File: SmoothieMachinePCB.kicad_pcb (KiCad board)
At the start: 2 copper layers, 50 parts, among them J1 Up Button, J10 Vin, J11 LCD I2C Adapter, J2 Down Button, J3 Next Ingredient Button, J4 Next Recipe Button, J5 Solenoid Valve, J6 Stepper Motor 2, J8 Stepper Motor 1, J9 LoadCell, U1 ESP32-S3-WROOM-2, U2 FSA2567MPX, U3 DRV8825PWP, U4 VN10KN3-G, U6 NAU7802SGI, U7 XL1509-3.3

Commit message: Second round pcb files
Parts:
- moved H3 109.1 mm to (88.6, 144.1)
- moved C2 84.3 mm to (94.5, 56.5), turned to -90 degrees
- moved H1 83.6 mm to (88.6, 51.1)
- moved J6 79.4 mm to (125.0, 116.6), turned to 90 degrees
- moved R12 79.0 mm to (110.0, 138.5), turned to -90 degrees
- moved C11 78.6 mm to (93.5, 131.5), turned to -90 degrees
- moved J10 73.0 mm to (88.2, 74.0)
- moved R3 73.0 mm to (105.0, 108.6)
- moved C10 72.6 mm to (99.5, 127.5), turned to -90 degrees
- moved R8 71.5 mm to (108.0, 128.0), turned to -90 degrees
- moved C12 70.4 mm to (102.5, 135.5), turned to -90 degrees
- moved L1 69.8 mm to (108.5, 57.5)
- moved J1 69.0 mm to (175.2, 58.0)
- moved U7 67.1 mm to (101.9, 59.0), turned to -90 degrees
- moved R11 67.0 mm to (124.0, 137.0), turned to -90 degrees
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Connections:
- D2 pad 1: /VDD33 -> Net-(D2-K)
- J11 pad 2: /VDD5 -> /VDD33
- L1 pad 1: /VDD33 -> Net-(D2-K)
- R3 pad 1: /MotorSelect -> /MOTORSELECT
- U7 pad 2: /VDD33 -> Net-(D2-K)
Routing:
- net /VDD33: track 0.00 -> 262.7 mm, vias 0 -> 6
- net +12V: track 0.00 -> 169.3 mm, vias 0 -> 6
- net /UP_BUTTON: track 0.00 -> 90.0 mm, vias 0 -> 4
- net /SOLENOID_VALVE: track 0.00 -> 77.5 mm, vias 0 -> 2
- net /MOTORSELECT: track 0.00 -> 64.4 mm, vias 0 -> 4
- net /DOWN_BUTTON: track 0.00 -> 60.2 mm
- net /DRDY: track 0.00 -> 57.6 mm, vias 0 -> 2
- net /SCLK: track 0.00 -> 56.5 mm, vias 0 -> 2
- net /BOUT2C: track 0.00 -> 56.1 mm, vias 0 -> 2
- net /DIR: track 0.00 -> 55.7 mm, vias 0 -> 2
- net /MODE1: track 0.00 -> 51.3 mm, vias 0 -> 2
- net /NRESET: track 0.00 -> 50.1 mm, vias 0 -> 2
- net /MODE2: track 0.00 -> 46.6 mm
- net /NEXT_RECEP_BUTTON: track 0.00 -> 46.5 mm, vias 0 -> 2
- net /AOUT1C: track 0.00 -> 46.2 mm, vias 0 -> 4
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- added copper zone on B.Cu, net +12V
- added copper zone on F.Cu, net +12V
- added copper zone on B.Cu, net /VDD33
- added copper zone on F.Cu, net /VDD33
- added copper zone on B.Cu, net GND
- added copper zone on F.Cu, net GND
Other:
- board outline added: 100 x 100 mm

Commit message: Labeled basically everything
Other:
- board text added: "SmoothieMachine 03-31-2025 Team 49"

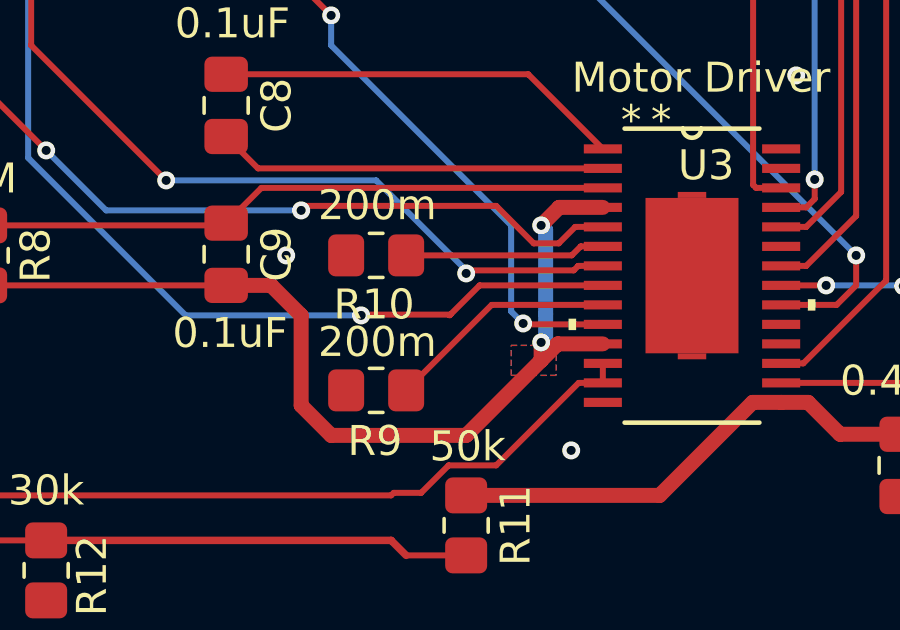
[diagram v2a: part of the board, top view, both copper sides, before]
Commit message: Integrated Microcontroller Essential Stuff into Schematic and Assigned Footprints
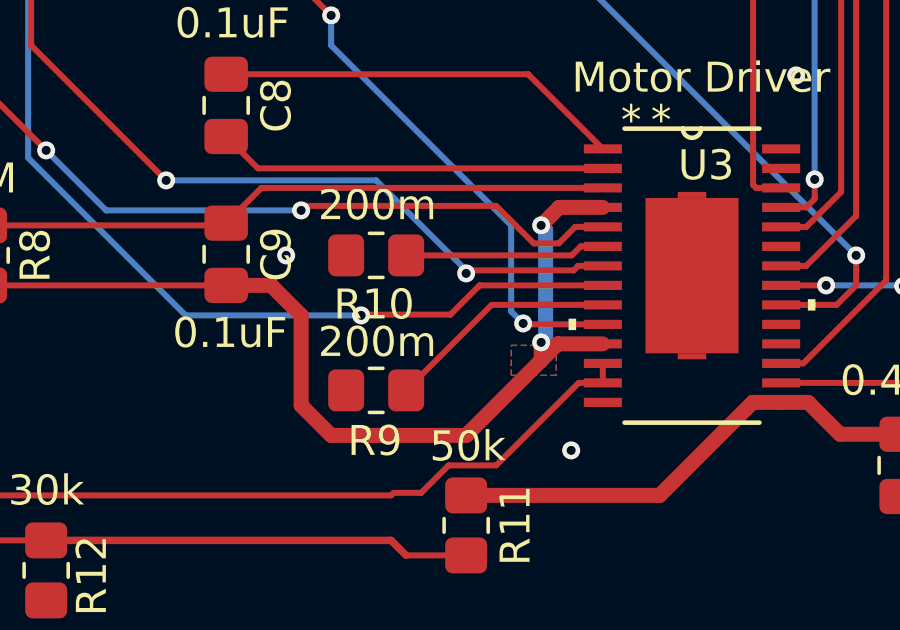
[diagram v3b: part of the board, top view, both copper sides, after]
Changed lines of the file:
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@@
 			(usegerberextensions no)
 			(usegerberattributes no)
-			(usegerberadvancedattributes yes)
-			(creategerberjobfile yes)
+			(usegerberadvancedattributes no)
+			(creategerberjobfile no)
 			(dashed_line_dash_ratio 12.000000)
 			(dashed_line_gap_ratio 3.000000)
@@
 			(psa4output no)
 			(plotreference yes)
-			(plotvalue yes)
+			(plotvalue no)
 			(plotfptext yes)
 			(plotinvisibletext no)
 			(sketchpadsonfab no)
-			(subtractmaskfromsilk no)
+			(subtractmaskfromsilk yes)
 			(outputformat 1)
 			(mirror no)
 			(drillshape 0)
 			(scaleselection 1)
-			(outputdirectory "")
+			(outputdirectory "ThirdWaveGerber/")
 		)
 	)
@@
 		(width 0.2)
 		(layer "F.Cu")
-		(net 66)
-	)
-	(segment
-		(start 123.474264 129.974264)
-		(end 123.448529 130)
-		(width 0.2)
-		(layer "F.Cu")

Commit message: Fourth wave ordered pcb files
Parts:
- removed L1: 47uH/3A, Inductor_SMD:L_0805_2012Metric_Pad1.05x1.20mm_HandSolder
- added C4: 1uF, Capacitor_SMD:C_0805_2012Metric_Pad1.18x1.45mm_HandSolder, F.Cu at (148.9, 110.2)
- added J12: Conn_ARM_JTAG_SWD_10, Connector_IDC:IDC-Header_2x05_P2.54mm_Vertical, F.Cu at (178.9, 111.5)
- added J13: Conn_01x06, Connector_Molex:Molex_KK-254_AE-6410-06A_1x06_P2.54mm_Vertical, F.Cu at (164.9, 115.2)
- added JP2: SolderJumper_2_Open, Jumper:SolderJumper-2_P1.3mm_Open_TrianglePad1.0x1.5mm, F.Cu at (112.6, 54.1)
- added JP3: SolderJumper_2_Open, Jumper:SolderJumper-2_P1.3mm_Open_TrianglePad1.0x1.5mm, F.Cu at (177.3, 120.3)
- added L2: PA4342.473NLT, PA4342.473NLT:IND_PA4342_FOOTPRINT2_PUL, F.Cu at (101.2, 59.3)
- added Q1: SS8050, Package_TO_SOT_SMD:SOT-23, F.Cu at (139.9, 110.6)
- added Q2: SS8050, Package_TO_SOT_SMD:SOT-23, F.Cu at (141.9, 121.0)
- added R15: 10k, Resistor_SMD:R_0805_2012Metric_Pad1.20x1.40mm_HandSolder, F.Cu at (147.0, 120.2)
- added R16: 10k, Resistor_SMD:R_0805_2012Metric_Pad1.20x1.40mm_HandSolder, F.Cu at (139.3, 115.9)
- added R17: 10k, Resistor_SMD:R_0805_2012Metric_Pad1.20x1.40mm_HandSolder, F.Cu at (141.7, 116.3)
- added R18: 0 ohm, Resistor_SMD:R_0805_2012Metric_Pad1.20x1.40mm_HandSolder, F.Cu at (145.6, 106.3)
- added R19: 0 ohm, Resistor_SMD:R_0805_2012Metric_Pad1.20x1.40mm_HandSolder, F.Cu at (143.1, 107.0)
- added R2: 1k, Resistor_SMD:R_0805_2012Metric_Pad1.20x1.40mm_HandSolder, F.Cu at (142.8, 102.4)
- added R4: 1k, Resistor_SMD:R_0805_2012Metric_Pad1.20x1.40mm_HandSolder, F.Cu at (144.9, 102.4)
- added R6: 100k, Resistor_SMD:R_0805_2012Metric_Pad1.20x1.40mm_HandSolder, F.Cu at (143.7, 111.9)
- added R7: 10k, Resistor_SMD:R_0805_2012Metric_Pad1.20x1.40mm_HandSolder, F.Cu at (143.8, 109.9)
- added SW1: SW_Push, Button_Switch_SMD:SW_SPST_B3S-1000, F.Cu at (155.4, 109.0)
- added SW2: SW_Push, Button_Switch_SMD:SW_SPST_B3S-1000, F.Cu at (155.4, 116.7)
- added TP1: TestPoint, TestPoint:TestPoint_Keystone_5010-5014_Multipurpose, F.Cu at (160.3, 138.1)
- added TP10: TestPoint, TestPoint:TestPoint_Keystone_5010-5014_Multipurpose, F.Cu at (89.7, 95.0)
- added TP11: TestPoint, TestPoint:TestPoint_Keystone_5010-5014_Multipurpose, F.Cu at (87.7, 84.6)
- added TP12: TestPoint, TestPoint:TestPoint_Keystone_5010-5014_Multipurpose, F.Cu at (97.1, 94.0)
- added TP13: TestPoint, TestPoint:TestPoint_Keystone_5010-5014_Multipurpose, F.Cu at (94.8, 121.3)
- added TP14: TestPoint, TestPoint:TestPoint_Keystone_5010-5014_Multipurpose, F.Cu at (179.4, 73.6)
- added TP15: TestPoint, TestPoint:TestPoint_Keystone_5010-5014_Multipurpose, F.Cu at (139.7, 106.8)
- added TP16: TestPoint, TestPoint:TestPoint_Keystone_5010-5014_Multipurpose, F.Cu at (138.8, 125.0)
- added TP17: TestPoint, TestPoint:TestPoint_Keystone_5010-5014_Multipurpose, F.Cu at (140.2, 129.4)
- added TP18: TestPoint, TestPoint:TestPoint_Keystone_5010-5014_Multipurpose, F.Cu at (104.9, 116.1)
- added TP19: TestPoint, TestPoint:TestPoint_Keystone_5010-5014_Multipurpose, F.Cu at (123.0, 120.6)
- added TP2: TestPoint, TestPoint:TestPoint_Keystone_5010-5014_Multipurpose, F.Cu at (114.0, 84.6)
- added TP20: TestPoint, TestPoint:TestPoint_Keystone_5010-5014_Multipurpose, F.Cu at (111.8, 119.8)
- added TP21: TestPoint, TestPoint:TestPoint_Keystone_5010-5014_Multipurpose, F.Cu at (106.0, 123.8)
- added TP22: TestPoint, TestPoint:TestPoint_Keystone_5010-5014_Multipurpose, F.Cu at (130.7, 106.2)
- added TP23: TestPoint, TestPoint:TestPoint_Keystone_5010-5014_Multipurpose, F.Cu at (132.9, 99.8)
- added TP24: TestPoint, TestPoint:TestPoint_Keystone_5010-5014_Multipurpose, F.Cu at (119.9, 96.8)
- added TP25: TestPoint, TestPoint:TestPoint_Keystone_5010-5014_Multipurpose, F.Cu at (122.6, 90.7)
- added TP26: TestPoint, TestPoint:TestPoint_Keystone_5010-5014_Multipurpose, F.Cu at (119.3, 116.8)
- added TP27: TestPoint, TestPoint:TestPoint_Keystone_5010-5014_Multipurpose, F.Cu at (130.7, 118.5)
- added TP28: TestPoint, TestPoint:TestPoint_Keystone_5010-5014_Multipurpose, F.Cu at (130.7, 114.2)
- added TP29: TestPoint, TestPoint:TestPoint_Keystone_5010-5014_Multipurpose, F.Cu at (130.6, 110.2)
- added TP3: TestPoint, TestPoint:TestPoint_Keystone_5010-5014_Multipurpose, F.Cu at (178.7, 93.5)
- added TP30: TestPoint, TestPoint:TestPoint_Keystone_5010-5014_Multipurpose, F.Cu at (159.0, 102.8)
- added TP31: TestPoint, TestPoint:TestPoint_Keystone_5010-5014_Multipurpose, F.Cu at (153.7, 131.5)
- added TP32: TestPoint, TestPoint:TestPoint_Keystone_5010-5014_Multipurpose, F.Cu at (160.2, 126.7)
- added TP33: TestPoint, TestPoint:TestPoint_Keystone_5010-5014_Multipurpose, F.Cu at (179.9, 126.9)
- added TP34: TestPoint, TestPoint:TestPoint_Keystone_5010-5014_Multipurpose, F.Cu at (110.4, 58.7)
- added TP35: TestPoint, TestPoint:TestPoint_Keystone_5010-5014_Multipurpose, F.Cu at (170.6, 116.6)
- added TP36: TestPoint, TestPoint:TestPoint_Keystone_5010-5014_Multipurpose, F.Cu at (170.6, 110.6)
- added TP37: TestPoint, TestPoint:TestPoint_Keystone_5010-5014_Multipurpose, F.Cu at (170.6, 105.9)
- added TP38: TestPoint, TestPoint:TestPoint_Keystone_5010-5014_Multipurpose, F.Cu at (160.9, 84.7)
- added TP4: TestPoint, TestPoint:TestPoint_Keystone_5010-5014_Multipurpose, F.Cu at (165.5, 79.6)
- added TP7: TestPoint, TestPoint:TestPoint_Keystone_5010-5014_Multipurpose, F.Cu at (182.8, 129.8)
- added TP8: TestPoint, TestPoint:TestPoint_Keystone_5010-5014_Multipurpose, F.Cu at (174.0, 81.5)
- added TP9: TestPoint, TestPoint:TestPoint_Keystone_5010-5014_Multipurpose, F.Cu at (170.4, 101.9)
- C11: footprint Capacitor_SMD:C_0805_2012Metric_Pad1.18x1.45mm_HandSolder -> UUD1C101MCL1GS:U2-I_NCH
- C2: footprint Capacitor_SMD:C_0805_2012Metric_Pad1.18x1.45mm_HandSolder -> EMK325ABJ107MM-T:CAP_EMK325AB_3P2X2P5_TAY
- C6: value 22uF -> 100nF
- C7: value 0.1uF -> 10uF
- C8: value 0.1uF -> 0.01uF
- R5: value 10k -> 100k
- moved C6 72.3 mm to (180.0, 122.8), turned to 90 degrees
- moved C7 70.9 mm to (182.3, 122.8), turned to 90 degrees
- moved C5 47.5 mm to (163.5, 119.0)
- moved J2 41.6 mm to (148.4, 101.7)
- moved J1 40.0 mm to (165.0, 96.7)
- moved R5 36.3 mm to (145.2, 115.4)
- moved J4 33.2 mm to (134.7, 88.6), turned to 180 degrees
- moved J3 31.4 mm to (135.9, 80.8), turned to 180 degrees
- moved C14 23.3 mm to (147.6, 132.0), turned to 0 degrees
- moved J9 21.0 mm to (156.2, 137.1), turned to 180 degrees
- moved C18 20.8 mm to (180.4, 133.3)
- moved C17 19.5 mm to (171.2, 125.3)
- moved R13 18.5 mm to (161.2, 130.1)
- moved U6 18.0 mm to (173.9, 133.8)
- moved C15 17.4 mm to (165.8, 131.8)
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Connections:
- net Net-(J9-Pin_2) renamed /LOADCELL2
- net Net-(J9-Pin_3) renamed /LOADCELL3
- net Net-(J9-Pin_4) renamed /LOADCELL4
- C1 pad 1: /VDD33 -> Net-(JP2-A)
- C5 pad 1: GND -> /GPIO0_STRAPPING
- C5 pad 2: Net-(U1-EN) -> GND
- R5 pad 2: Net-(U1-EN) -> /GPIO0_STRAPPING
- U1 pad 15: /MODE0 -> /GPIO3_STRAPPING
- U1 pad 16: /NSLEEP -> /GPIO46_STRAPPING
- U1 pad 27: unconnected-(U1-IO0-Pad27) -> /GPIO0_STRAPPING
- U1 pad 3: Net-(U1-EN) -> /CHIP_PU
- U1 pad 32: unconnected-(U1-MTCK/IO39-Pad32) -> /MTCK
- U1 pad 33: unconnected-(U1-MTDO/IO40-Pad33) -> /MTDO
- U1 pad 34: unconnected-(U1-MTDI/IO41-Pad34) -> /MTDI
- U1 pad 35: unconnected-(U1-MTMS/IO42-Pad35) -> /MTMS
- U1 pad 36: unconnected-(U1-RXD0/IO44-Pad36) -> /RX
- U1 pad 37: unconnected-(U1-TXD0/IO43-Pad37) -> /TX
- U1 pad 6: unconnected-(U1-IO6-Pad6) -> /NSLEEP
- U1 pad 7: unconnected-(U1-IO7-Pad7) -> /MODE0
- U7 pad 3: /VDD33 -> Net-(JP2-A)
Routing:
- net /CHIP_PU: track 0.00 -> 82.5 mm, vias 0 -> 2
- net /UP_BUTTON: track 90.0 -> 17.3 mm, vias 4 -> 1
- net /RTS: track 0.00 -> 56.2 mm, vias 0 -> 1
- net /DOWN_BUTTON: track 60.2 -> 6.15 mm
- net /VDD33: track 262.7 -> 313.2 mm, vias 6 -> 8
- net /GPIO0_STRAPPING: track 0.00 -> 46.5 mm, vias 0 -> 2
- net Net-(JP2-A): track 0.00 -> 42.5 mm, vias 0 -> 2
- net /DTR: track 0.00 -> 42.2 mm, vias 0 -> 1
- net /NEXT_RECEP_BUTTON: track 46.5 -> 5.35 mm, vias 2 -> 1
- net /TX: track 0.00 -> 39.5 mm, vias 0 -> 1
- net /MTMS: track 0.00 -> 38.7 mm, vias 0 -> 1
- net /MTCK: track 0.00 -> 33.7 mm, vias 0 -> 1
- net GND: track 12.0 -> 45.5 mm, vias 13 -> 28
- net Net-(U3-AVREF): track 41.9 -> 9.71 mm
- net /MTDO: track 0.00 -> 32.0 mm, vias 0 -> 1
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
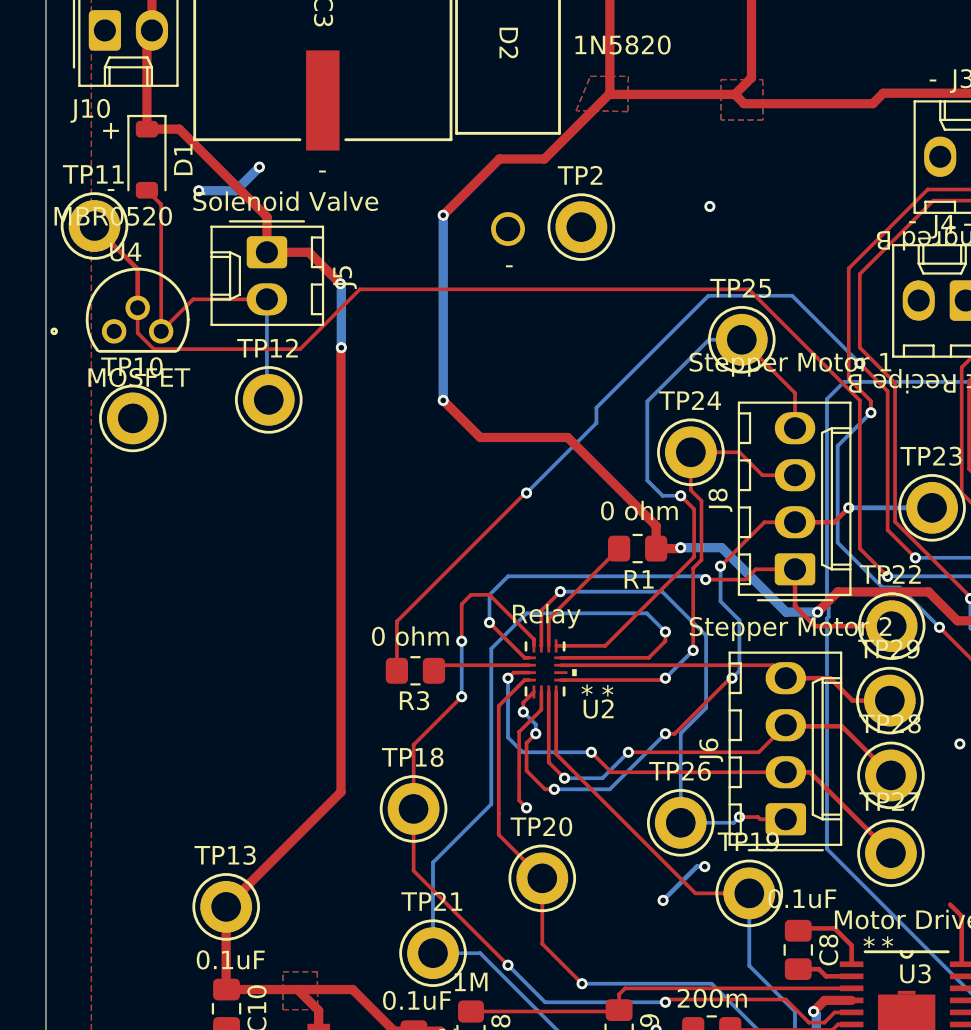
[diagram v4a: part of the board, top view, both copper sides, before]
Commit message: Fixed incorrect capacitor value
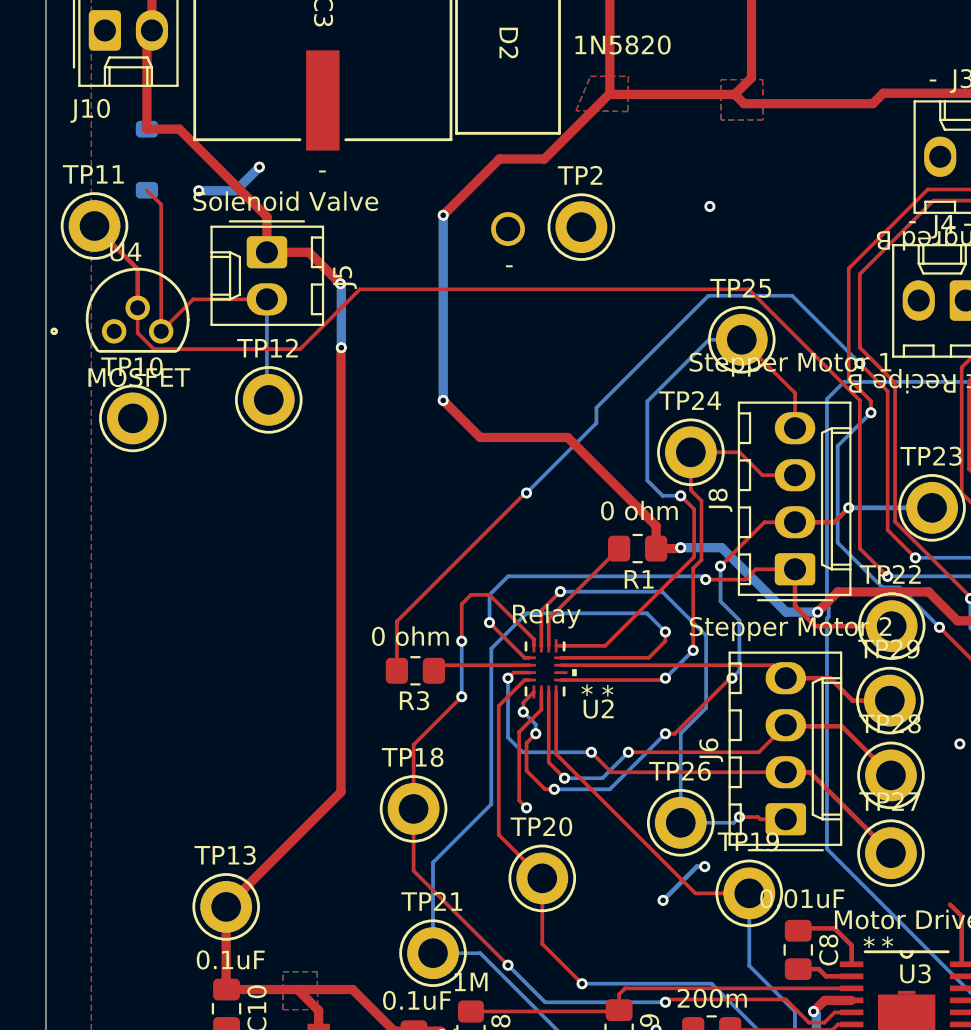
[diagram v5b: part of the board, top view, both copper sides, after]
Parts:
- D1: moved to B.Cu
